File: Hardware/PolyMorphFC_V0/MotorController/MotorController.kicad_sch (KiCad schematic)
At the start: 90 parts, among them J1 Conn_01x03_Pin, J2 Conn_01x02_Pin, J3 Conn_01x02_Pin, J4 Conn_01x02_Pin, J5 Conn_01x06_Pin, Q1 BSC028N06NS, Q2 BSC028N06NS, Q3 BSC028N06NS, Q4 BSC028N06NS, Q5 BSC028N06NS, Q6 BSC028N06NS, SW1 SW_Push, U1 STM32G474RET6, U2 DRV8305NPHPR, U3 WS2812C-2020, U4 LMR33620BDDAR, U5 AS5048A, U6 WS2812C-2020

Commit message: Schematic OK & Setup FOC Controller board firmware using STM IDE (C / C++)
-   Using RUST for Low Level firmware creates a lot of software archiecture constraints not compatible with ergonomic system -   A rework in Rust could be considered in the future
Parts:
- removed C21: 4.7uF, symbol Device:C
- removed C22, C45: 1uF, symbol Device:C
- removed C24, C29, C30, C31, C32, C34: 330uF, symbol Device:C
- removed C28, C46, C47: 10uF, symbol Device:C
- removed C35: 10nF, symbol Device:C
- removed C36, C39, C41, C42, C43, C44: 0.1uF, symbol Device:C
- removed C37, C38: 220uF, symbol Device:C
- removed C4, C5: 470uF, symbol Device:C_Polarized
- removed D1, D2, D3, D4: D_Zener, symbol Device:D_Zener
- removed J2, J4: Conn_01x02_Pin, symbol Connector:Conn_01x02_Pin
- removed L2: 2.2uF, symbol Device:L
- removed R5: 10kΩ, symbol Device:R
- removed U1: STM32G474RET6, Package_QFP:LQFP-64_10x10mm_P0.5mm, symbol MCU_ST_STM32G4:STM32G474RETx
- removed U2: DRV8305NPHPR, DRV8305NPHPR:PHP0048G_N, symbol DRV8305NPHPR:DRV8305NPHPR
- removed U3, U6: WS2812C-2020, SMT_2C-2020_WDS, symbol WS2812C-2020:WS2812C-2020
- removed U4: LMR33620BDDAR, DDA0008J, symbol LMR33620CDDAR:LMR33620CDDAR
- added C4: 0.1uF, Capacitor_SMD:C_0402_1005Metric, symbol Device:C
- added C5: 1uF, Capacitor_SMD:C_0402_1005Metric, symbol Device:C
- added D1, D2, D3, D6, D7, D9: D_Schottky, Diode_SMD:D_SOD-123F, symbol Device:D_Schottky
- added D10, D11, D12, D8: LED, LED_SMD:LED_0603_1608Metric, symbol Device:LED
- added D4: ~, Diode_SMD:D_2010_5025Metric, symbol Device:D
- added J6: Conn_01x02_Pin, Connector_AMASS:AMASS_XT60PW-M_1x02_P7.20mm_Horizontal, symbol Connector:Conn_01x02_Pin
- added R2, R20, R21, R26: 120Ω, Resistor_SMD:R_0402_1005Metric, symbol Device:R
- added R22, R23, R24, R25: 10Ω, Resistor_SMD:R_0402_1005Metric, symbol Device:R
- added R5: 10kΩ, Resistor_SMD:R_0402_1005Metric, symbol Device:R_Variable
- added U1: STSPIN32G4, STSPIN32G4:QFN_IN32G4_STM, symbol STSPIN32G4:STSPIN32G4
- C1: footprint (none) -> Capacitor_SMD:C_0402_1005Metric; Component (none) -> 0402B102K500NT
- C10, C13: value 22uF -> 100nF; footprint (none) -> Capacitor_SMD:C_0402_1005Metric; Component CL31B106KBHNNNE -> GRM155R61H105KE05D
- C11: value 1uF -> 33nF; footprint (none) -> Capacitor_SMD:C_0402_1005Metric; Component CL31B106KBHNNNE -> GRM155R61H105KE05D
- C12: value 10uF -> 33nF; footprint (none) -> Capacitor_SMD:C_0402_1005Metric; Component CL31B106KBHNNNE -> GRM155R61H105KE05D
- C14: value 220nF -> 1uF; footprint (none) -> Capacitor_SMD:C_0402_1005Metric; Component CL31B106KBHNNNE -> GRM155R61H105KE05D
- C15, C17: value 1uF -> 100nF; footprint (none) -> Capacitor_SMD:C_0402_1005Metric; Component EEEFT1H331AP -> GRM155R61H105KE05D
- C16: value 1uF -> 10uF; footprint (none) -> Capacitor_SMD:C_0402_1005Metric; Component EEEFT1H331AP -> GRM155R61H105KE05D
- C18: value 47nF -> 10uF; footprint (none) -> Capacitor_SMD:C_0402_1005Metric; Component EEEFT1H331AP -> GRM155R61H105KE05D
- C19: value 47nF -> 1uF; footprint (none) -> Capacitor_SMD:C_0402_1005Metric; Component EEEFT1H331AP -> GRM155R61H105KE05D
- C2, C3: value 0.1uF -> 1uF; footprint (none) -> Capacitor_SMD:C_0402_1005Metric; Component (none) -> GRM155R61H105KE05D
- C20: value 2.2uF -> 0.1uF; footprint (none) -> Capacitor_SMD:C_0402_1005Metric; Component EEEFT1H331AP -> 0402B102K500NT
- C23: footprint (none) -> Capacitor_SMD:C_Elec_10x10.2
- C25: value 330uF -> 1uF; footprint (none) -> Capacitor_SMD:C_0402_1005Metric; Component EEEFT1H331AP -> GRM155R61H105KE05D
- C26: value 10uF -> 330uF; footprint (none) -> Capacitor_SMD:C_Elec_10x10.2; Component CL31B106KBHNNNE -> EEEFT1H331AP
- C27: value 10uF -> 1uF; footprint (none) -> Capacitor_SMD:C_0402_1005Metric; Component CL31B106KBHNNNE -> GRM155R61H105KE05D
- C33: value 330uF -> 0.1uF; footprint (none) -> Capacitor_SMD:C_0402_1005Metric; Component EEEFT1H331AP -> 0402B102K500NT
- C40: footprint (none) -> Capacitor_SMD:C_1206_3216Metric; Component (none) -> CL31A106KBHNNNE
- C6: value 0.1uF -> 1uF; footprint (none) -> Capacitor_SMD:C_0402_1005Metric; Component EEEFT1H331AP -> GRM155R61H105KE05D
- C7: value 0.1uF -> 100nF; footprint (none) -> Capacitor_SMD:C_0402_1005Metric; Component CL31B106KBHNNNE -> GRM155R61H105KE05D
- C8: value 0.1uF -> 330uF; footprint (none) -> Capacitor_SMD:C_Elec_10x10.2; Component CL31B106KBHNNNE -> EEEFT1H331AP
- C9: value 0.1uF -> 220nF; footprint (none) -> Capacitor_SMD:C_0402_1005Metric; Component CL31B106KBHNNNE -> GRM155R61H105KE05D
- D5: value PTVSHC1TF24VU -> ~; Component (none) -> PTVSHC1TF24VU
- J1: footprint (none) -> Connector_AMASS:MR60PW
- J3: footprint (none) -> Connector_AMASS:AMASS_XT60-F_1x02_P7.20mm_Vertical
- J5: value Conn_01x06_Pin -> JST_XH_01x06; footprint (none) -> Connector_JST:JST_XH_S6B-XH-SM4-TB_1x06-1MP_P2.50mm_Horizontal
- L1: value L -> 18uH; footprint (none) -> Inductor_SMD:L_1008_2520Metric; Component (none) -> SM3521-2R2MT
- Q1, Q2, Q3, Q4, Q5, Q6: value BSC028N06NS -> BSC016N06NS; footprint Package_TO_SOT_SMD:TDSON-8-1 -> Package_SON:Infineon_PG-TDSON-8_6.15x5.15mm
- R1: value 10kΩ -> 100kΩ; footprint (none) -> Resistor_SMD:R_0603_1608Metric; Component (none) -> 0603WAJ0103T5E
- R10, R12: value 35kΩ -> 15Ω; footprint (none) -> Resistor_SMD:R_0402_1005Metric; Component (none) -> 0402WGF150JTCE
- R11, R15: value 5kΩ -> 5mΩ; footprint (none) -> Resistor_SMD:R_4527_11375MetricL; Component (none) -> LR4527-25R005FA
- R13: value 5kΩ -> 15Ω; footprint (none) -> Resistor_SMD:R_0402_1005Metric; Component (none) -> 0402WGF150JTCE
- R14: value 35kΩ -> 5mΩ; footprint (none) -> Resistor_SMD:R_4527_11375MetricL; Component (none) -> LR4527-25R005FA
- R16: value 35kΩ -> 1.2kΩ; footprint (none) -> Resistor_SMD:R_0402_1005Metric; Component (none) -> 0402WGF1201TCE
- R17: value 5kΩ -> 10kΩ; footprint (none) -> Resistor_SMD:R_0603_1608Metric; Component (none) -> 0603WAJ0103T5E
- R18: value 43.2kΩ -> 10Ω; footprint (none) -> Resistor_SMD:R_0402_1005Metric; Component (none) -> 0402WGF100JTCE
- R19: value 100kΩ -> 10Ω; footprint (none) -> Resistor_SMD:R_0402_1005Metric; Component (none) -> 0402WGF100JTCE
- R3: value 100kΩ -> 10kΩ; footprint (none) -> Resistor_SMD:R_0603_1608Metric; Component (none) -> 0603WAJ0103T5E
- R4: footprint (none) -> Resistor_SMD:R_0603_1608Metric; Component (none) -> 0603WAJ0103T5E
- R6: value 100Ω -> 10kΩ; footprint (none) -> Resistor_SMD:R_0603_1608Metric; Component (none) -> 0603WAJ0103T5E
- R7, R8, R9: value 5mΩ -> 15Ω; footprint (none) -> Resistor_SMD:R_0402_1005Metric; Component (none) -> 0402WGF150JTCE
- SW1: footprint (none) -> Button_Switch_SMD:SW_Push_1TS009xxxx-xxxx-xxxx_6x6x5mm; Component (none) -> SPEH110100
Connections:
- net PG is gone; now on an unnamed net: R19.2
- net +3V3: now also C33.1; no longer C10.1, C13.1, C16.1, C8.2, L1.1, R3.1, R4.1
- net +BATT: now also C13.2, C14.2, C15.2, C2.2, C23.2, C25.2, C26.2, C6.2, C7.2, C8.2, R1.2, C5.2, J6.1 (Pin_1), R5.1, U1.2 (VBAT), U1.26 (VREF+), U1.27 (VDDA); no longer C12.1, C14.1, C20.2, C26.1, C27.1, C6.1, Q1.5 (D), Q3.5 (D), Q5.5 (D), R16.1
- net GND: now also C10.1, C11.1, C12.1, C13.1, C14.1, C16.1, C18.1, C19.1, C23.1, C26.1, C27.1, C3.1, C6.1, C7.1, C9.1, R14.2, R16.1, R17.1, R3.1, D10.1 (K), D11.1 (K), D12.1 (K), D4.2 (A), D8.1 (K), J6.2 (Pin_2), U1.15 (PA2), U1.20 (PA7), U1.24 (PB1), U1.32 (PGND); no longer C1.2, C10.2, C11.2, C12.2, C13.2, C14.2, C2.2, C23.2, C25.2, C26.2, C27.2, C3.2, C6.2, C7.2, R1.2, R13.2, R17.2, R18.2, R7.2, R8.2, R9.2
- net MAG_PWM: now also U1.45 (PA9)
- net NRST: no longer C7.1, SW1.2
- net SPI_MAG_CLK: now also U1.7 (PF1)
- net SPI_MAG_CS: now also U1.6 (PF0)
- net SPI_MAG_MISO: now also U1.46 (PA10)
- net SPI_MAG_MOSI: now also U1.47 (PA11)
- net SWCLK: now also U1.50 (PA14)
- net SWDIO: now also U1.49 (PA13)
- net SWO: now also U1.54 (PB3)
- net VCC: now also U1.63 (VCC)
- net at R18.1: now also D9.2 (A); no longer R3.2
- net at R19.1: now also D1.2 (A); no longer C11.1
- net VM: now reaches C9.2
- net VM: now also R4.2, U1.61 (VM)
- net at R1.1: now also C10.2, SW1.2, U1.8 (PG10)
- net at L1.2: now also C18.2, U1.62 (SW)
- net BOOT3: now reaches C20.1
- net BOOT3: now also U1.35 (BOOT3)
- net at C17.2: now also C16.2, U1.1 (REG3V3/VDD)
- net Shunt_H2: now reaches C19.2
- net Shunt_H2: now also Q4.1 (S), Q4.2 (S), Q4.3 (S), R11.1, U1.19 (PA6)
- net at R6.1: now also R17.2, U1.52 (SCREF)
- removed net A_SENSE: C1.1, R10.2, R11.1
- removed net B_SENSE: C2.1, R12.2, R13.1
- removed net C_SENSE: C3.1, R14.2, R15.1
- net GH_A: no longer names the net of Q1.4 (G)
- net GH_A: now also R18.2, R7.2
- net GH_B: no longer names the net of Q3.4 (G)
- net GH_B: now also R8.2, R22.2
- net GH_C: no longer names the net of Q5.4 (G)
- net GH_C: now also R12.2, R24.2
- net GL_A: no longer names the net of Q2.4 (G)
- net GL_A: now also R10.2
- net GL_B: no longer names the net of Q4.4 (G)
- net GL_B: now also R9.2, R23.2
- net GL_C: no longer names the net of Q6.4 (G)
- net GL_C: now also R13.2, R25.2
- net PHASE_A renamed OUT1
- net OUT1: now also C1.2, U1.42 (OUT1); no longer R10.1
- net PHASE_B renamed OUT2
- net OUT2: now also C4.2, U1.39 (OUT2); no longer R12.1
- net PHASE_C renamed OUT3
- net OUT3: now also C20.2, U1.36 (OUT3); no longer R14.1
- net PVDD_SENSE: no longer names the net of R16.2
- net PVDD_SENSE: now also C12.2, R5.2, U1.21 (PC4); no longer R17.1
- net SL_A renamed Shunt_H1
- net Shunt_H1: now also C3.2, R15.1, U1.14 (PA1); no longer C23.1, R7.1
- removed net SL_B: Q4.1 (S), Q4.2 (S), Q4.3 (S), R8.1
- net SL_C renamed Shunt_H3
- net Shunt_H3: now also C27.2, R14.1, U1.23 (PB0); no longer C25.1, C33.1, R9.1
- new net: D10.2 (A), R26.2
- new net: D6.2 (A), R24.1
- new net: C25.1, Q5.5 (D)
- new net: D11.2 (A), R20.2
- new net: D2.2 (A), R22.1
- new net: C5.1, Q3.5 (D)
- new net: C11.2, R3.2, R4.1, U1.13 (PA0)
- new net: C2.1, Q1.5 (D)
- new net: D7.2 (A), R25.1
- new net: D3.2 (A), R23.1
- new net: D4.1 (K), L1.1, U1.64 (REGIN)
- new net: D8.2 (A), R2.2
- new net: D12.2 (A), R21.2
- new net BOOT1: C1.1, U1.41 (BOOT1)
- new net BOOT2: C4.1, U1.38 (BOOT2)
- new net GHS1: D9.1 (K), R7.1, U1.43 (GHS1)
- new net GHS2: D2.1 (K), R8.1, U1.40 (GHS2)
- new net GHS3: D6.1 (K), R12.1, U1.37 (GHS3)
- new net GLS1: D1.1 (K), R10.1, U1.29 (GLS1)
- new net GLS2: D3.1 (K), R9.1, U1.30 (GLS2)
- new net GLS3: D7.1 (K), R13.1, U1.31 (GLS3)
- new net JTDI: U1.51 (PA15)
- new net LED0_Output: R26.1, U1.57 (PB6)
- new net LED1_Output: R2.1, U1.58 (PB7)
- new net LED2_Output: R20.1, U1.59 (PB8)
- new net LED3_Output: R21.1, U1.60 (PB9)
- new net LPUART_RX: U1.9 (PC0)
- new net LPUART_TX: U1.10 (PC1)
- no-connect marks 6 -> 5
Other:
- moved on the sheet: D5, J1, J3, J5, U5

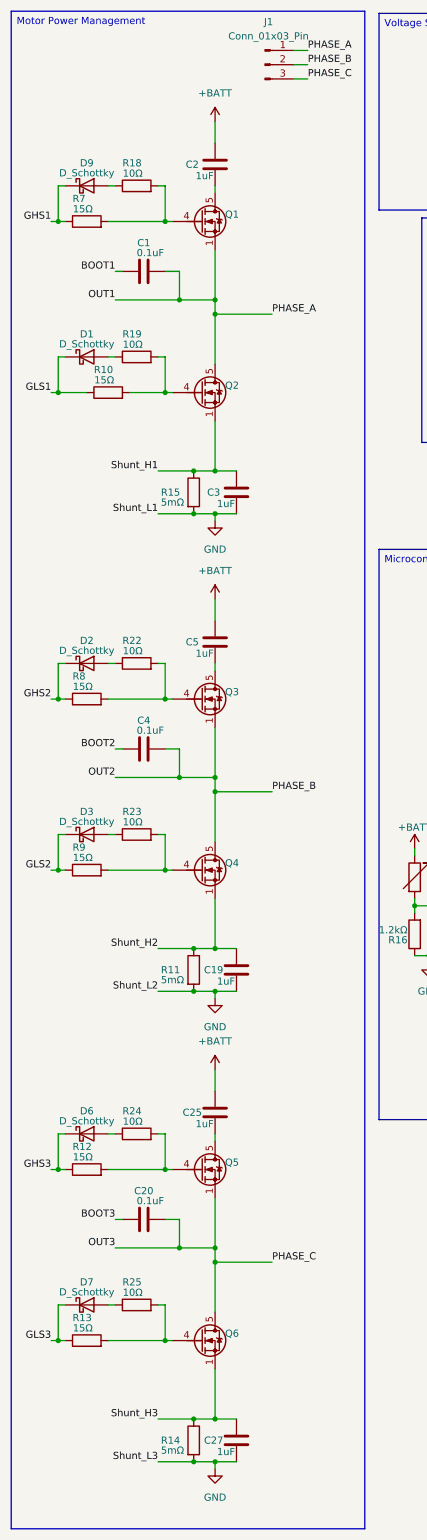
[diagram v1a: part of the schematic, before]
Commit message: Footprint placements and screens
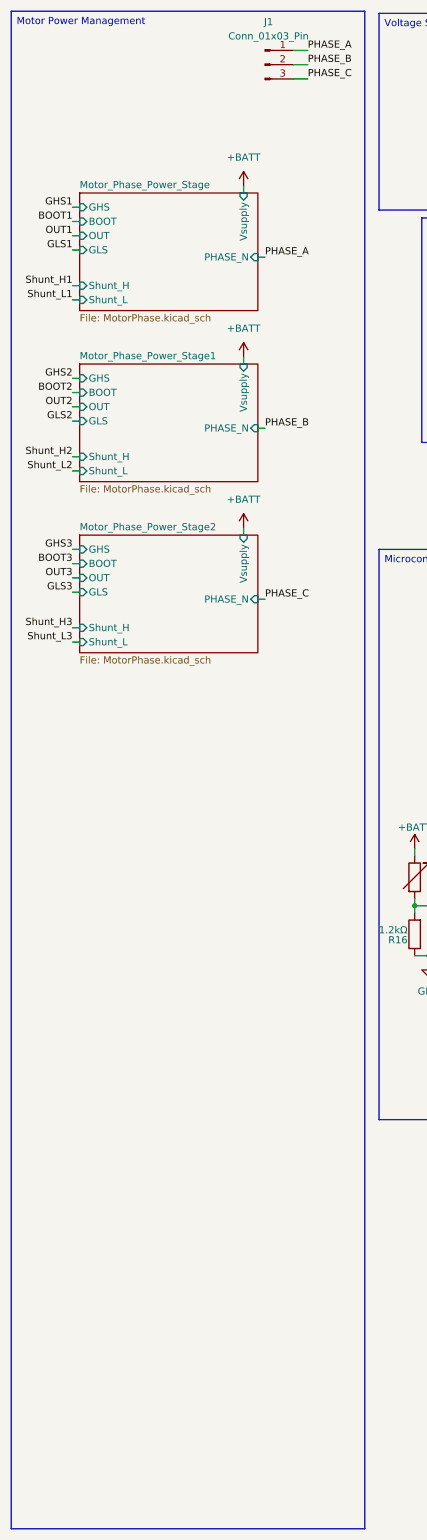
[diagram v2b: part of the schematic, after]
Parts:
- removed C1, C20, C4: 0.1uF, Capacitor_SMD:C_0402_1005Metric, symbol Device:C
- removed C19, C2, C25, C27, C3, C5: 1uF, Capacitor_SMD:C_0402_1005Metric, symbol Device:C
- removed D1, D2, D3, D6, D7, D9: D_Schottky, Diode_SMD:D_SOD-123F, symbol Device:D_Schottky
- removed Q1, Q2, Q3, Q4, Q5, Q6: BSC016N06NS, Package_SON:Infineon_PG-TDSON-8_6.15x5.15mm, symbol Transistor_FET:BSC040N08NS5
- removed R10, R12, R13, R7, R8, R9: 15Ω, Resistor_SMD:R_0402_1005Metric, symbol Device:R
- removed R11, R14, R15: 5mΩ, Resistor_SMD:R_4527_11375MetricL, symbol Device:R
- removed R18, R19, R22, R23, R24, R25: 10Ω, Resistor_SMD:R_0402_1005Metric, symbol Device:R
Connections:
- net GND: no longer U1.15 (PA2), U1.20 (PA7), U1.24 (PB1)
- net OUT1: no longer J1.1 (Pin_1)
- net OUT2: no longer J1.2 (Pin_2)
- net OUT3: no longer J1.3 (Pin_3)
- new net PHASE_A: J1.1 (Pin_1)
- new net PHASE_B: J1.2 (Pin_2)
- new net PHASE_C: J1.3 (Pin_3)
- new net Shunt_L1: U1.15 (PA2)
- new net Shunt_L2: U1.20 (PA7)
- new net Shunt_L3: U1.24 (PB1)
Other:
- added sheet Motor_Phase_Power_Stage (MotorPhase.kicad_sch)
- added sheet Motor_Phase_Power_Stage1 (MotorPhase.kicad_sch)
- added sheet Motor_Phase_Power_Stage2 (MotorPhase.kicad_sch)
